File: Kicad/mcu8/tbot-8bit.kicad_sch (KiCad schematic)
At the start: 8 parts

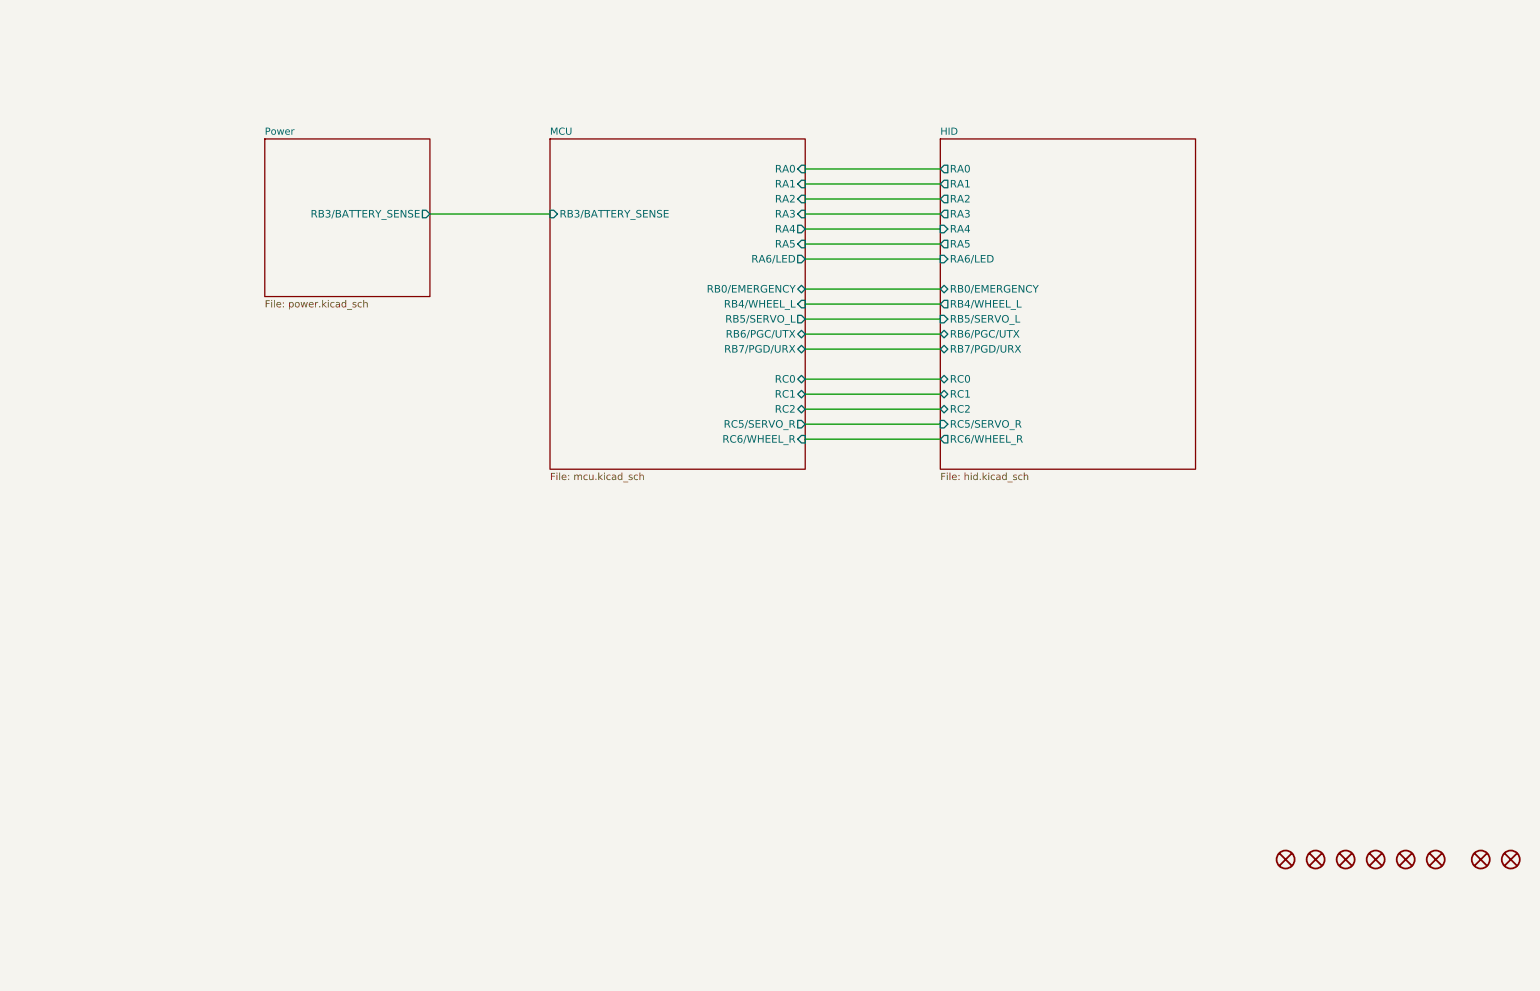
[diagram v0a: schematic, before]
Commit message: Update MCU 8Bit
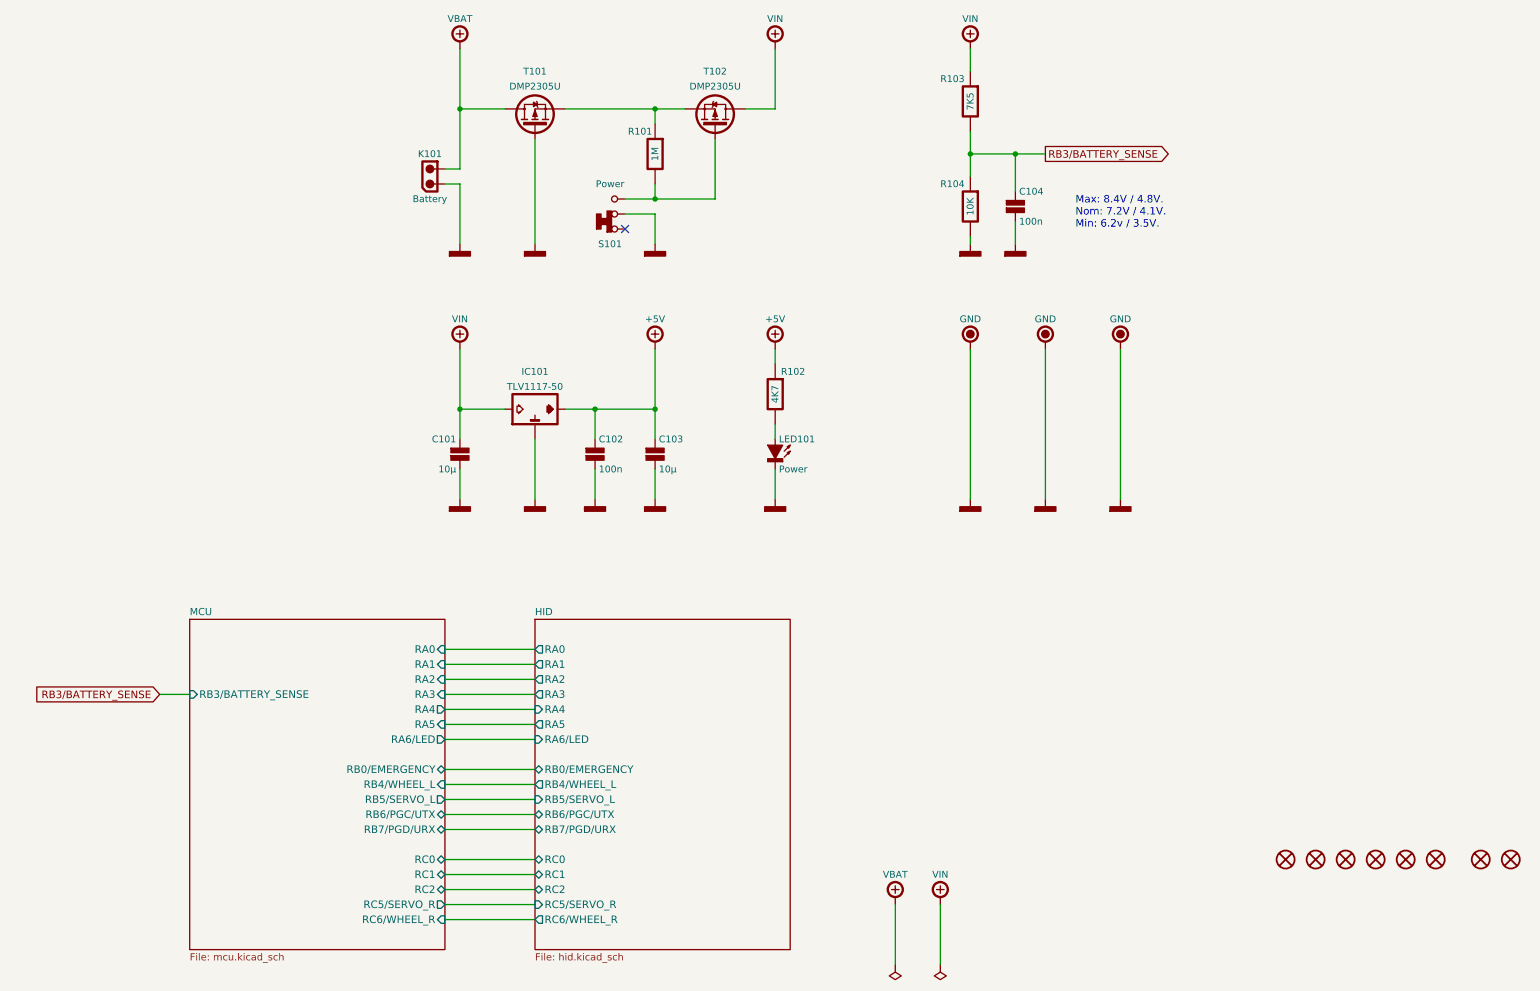
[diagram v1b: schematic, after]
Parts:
- added C101, C103: 10µ, tronixio:CAPACITOR-1206, symbol tronixio:C-1206
- added C102, C104: 100n, tronixio:CAPACITOR-1206, symbol tronixio:C-1206
- added IC101: TLV1117-50, tronixio:SOT-223-3, symbol tronixio:TLV1117-50-SOT
- added K101: Battery, tronixio:MOLEX-22057025, symbol tronixio:MOLEX-MINI-SPOX-02-RIGHT-ANGLE
- added LED101: Power, tronixio:LED-1206, symbol tronixio:LED-1206-PURPLE
- added R101: 1M, tronixio:RESISTOR-1206, symbol tronixio:R-1206
- added R102: 4K7, tronixio:RESISTOR-1206, symbol tronixio:R-1206
- added R103: 7K5, tronixio:RESISTOR-1206, symbol tronixio:R-1206
- added R104: 10K, tronixio:RESISTOR-1206, symbol tronixio:R-1206
- added S101: Power, tronixio:E-SWITCH-200USPXT1A1M2RE, symbol tronixio:E-SWITCH-200USP1T1A1M2RE
- added T101, T102: DMP2305U, tronixio:SOT-23-3, symbol tronixio:DMP2305U-NEW
- added TP101, TP102, TP103: GND, tronixio:KEYSTONE-5006, symbol tronixio:KEYSTONE-5006
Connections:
- new net: LED101.2 (A), R102.1
- new net: R101.1, S101.3, T102.1 (G)
- new net: R101.2, T101.2 (S), T102.2 (S)
- new net +5V: C102.1, C103.1, IC101.2 (VO), R102.2
- new net GND: C101.2, C102.2, C103.2, C104.2, IC101.1 (GND), K101.1, LED101.1 (K), R104.1, S101.2, T101.1 (G), TP101.1, TP102.1, TP103.1
- new net RB3/BATTERY_SENSE: C104.1, R103.1, R104.2
- new net VBAT: K101.2, T101.3 (D)
- new net VIN: C101.1, IC101.3 (VI), R103.2, T102.3 (D)
- no-connect marks 0 -> 1
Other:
- removed sheet Power
- note added: "Max: 8.4V / 4.8V. Nom: 7.2V / 4.1V. Min: 6.2v / 3.5V."

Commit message: Update tbot-8bit.kicad_sch
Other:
- title: Diagram -> Power
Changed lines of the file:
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@@
   (paper "A4")
   (title_block
-    (title "Diagram")
+    (title "Power")
     (date "01/2022")
     (rev "A")
@@
   (sheet_instances
     (path "/" (page "1"))
-    (path "/6012b3a0-2f30-4458-8240-bd443182c6c0" (page "3"))
-    (path "/56bd3a46-de12-45e9-9566-afec966f2cad" (page "4"))
+    (path "/6012b3a0-2f30-4458-8240-bd443182c6c0" (page "2"))
+    (path "/56bd3a46-de12-45e9-9566-afec966f2cad" (page "3"))
   )
   (symbol_instances

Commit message: Update tbot-8bit.kicad_sch
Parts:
- removed TP103: GND, tronixio:KEYSTONE-5006, symbol tronixio:KEYSTONE-5006
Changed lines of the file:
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@@
     (stroke (width 0) (type default) (color 0 0 0 0))
-  )
-  (wire (pts (xy 210.82 86.36) (xy 210.82 111.76))
-    (stroke (width 0) (type solid) (color 0 0 0 0))
   )
   (wire (pts (xy 96.52 139.7) (xy 111.76 139.7))
@@
     )
   )
-  (symbol (lib_id "tronixio:KEYSTONE-5006") (at 210.82 86.36 0) (unit 1)
-    (in_bom yes) (on_board yes)
-    (property "Reference" "TP103" (id 0) (at 210.82 93.98 0)
-      (effects (font (size 1.15 1.15)) hide)
-    )
-    (property "Value" "GND" (id 1) (at 210.82 81.28 0)
-      (effects (font (size 1.15 1.15)))
-    )
-    (property "Footprint" "tronixio:KEYSTONE-5006" (id 2) (at 210.82 96.52 0)
-      (effects (font (size 1 1)) hide)
-    )
-    (property "Datasheet" "https://www.keyelco.com/product.cfm/product_id/1315" (id 3) (at 210.82 99.06 0)
-      (effects (font (size 1 1)) hide)
-    )
-    (property "MOUSER" "534-5006" (id 4) (at 210.82 101.6 0)
-      (effects (font (size 1 1)) hide)
-    )
-    (pin "1")
-  )
   (symbol (lib_id "tronixio:MOUNTING-HOLE-MASK-3MM") (at 264.16 172.72 0) (unit 1)
     (in_bom yes) (on_board yes)
@@
     )
     (property "Datasheet" "" (id 3) (at 99.06 111.76 0)
-      (effects (font (size 1 1)) hide)
-    )
-    (pin "1")
-  )
-  (symbol (lib_id "tronixio:POWER-GND") (at 210.82 111.76 0) (unit 1)
-    (in_bom yes) (on_board yes)
-    (property "Reference" "#PWR0121" (id 0) (at 210.82 118.11 0)
-      (effects (font (size 1 1)) hide)
-    )
-    (property "Value" "GND" (id 1) (at 210.82 115.57 0)
-      (effects (font (size 1 1)) hide)
-    )
-    (property "Footprint" "" (id 2) (at 210.82 111.76 0)
-      (effects (font (size 1 1)) hide)
-    )
-    (property "Datasheet" "" (id 3) (at 210.82 111.76 0)
       (effects (font (size 1 1)) hide)
     )
@@
       (reference "#PWR0120") (unit 1) (value "GND") (footprint "")
     )
-    (path "/63226fa0-632d-4ce6-8a17-8a058e81c611"
-      (reference "#PWR0121") (unit 1) (value "GND") (footprint "")
-    )
     (path "/6012b3a0-2f30-4458-8240-bd443182c6c0/897b9fb4-999f-4b4b-be60-8182d70f5116"
       (reference "#PWR0301") (unit 1) (value "+5V") (footprint "")
@@
       (reference "TP102") (unit 1) (value "GND") (footprint "tronixio:KEYSTONE-5006")
     )
-    (path "/0f01468d-4793-40a9-aa18-d4ec9b5eefff"
-      (reference "TP103") (unit 1) (value "GND") (footprint "tronixio:KEYSTONE-5006")
-    )
-  )
+  )

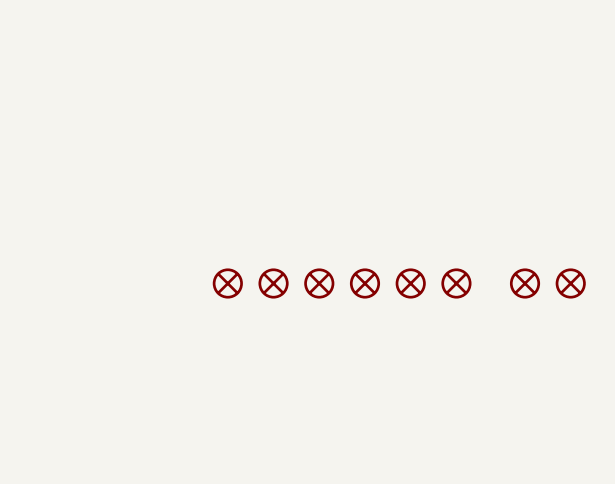
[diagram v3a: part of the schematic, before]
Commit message: Update MCU 8Bit
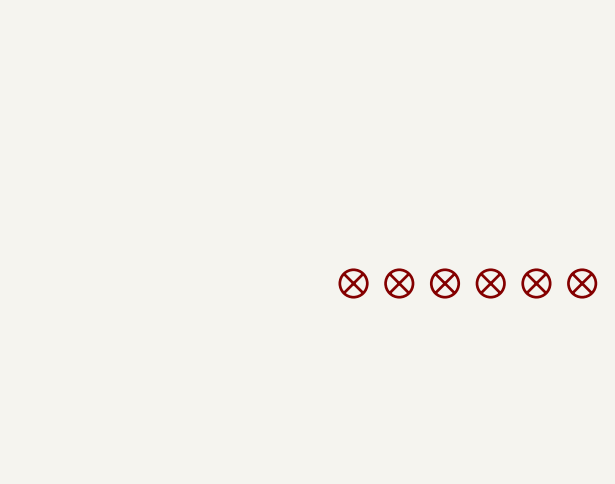
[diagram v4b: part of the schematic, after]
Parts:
- removed H107, H108: MOUNTING-HOLE-3MM, tronixio:M3, symbol tronixio:MOUNTING-HOLE-3MM
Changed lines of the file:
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@@
     )
   )
-  (symbol (lib_id "tronixio:MOUNTING-HOLE-MASK-3MM") (at 264.16 172.72 0) (unit 1)
-    (in_bom yes) (on_board yes)
-    (property "Reference" "H106" (id 0) (at 264.16 167.64 0)
-      (effects (font (size 1 1)) hide)
-    )
-    (property "Value" "MOUNTING-HOLE-MASK-3MM" (id 1) (at 264.16 170.18 0)
-      (effects (font (size 1 1)) hide)
-    )
-    (property "Footprint" "tronixio:M3-MASK" (id 2) (at 264.16 175.26 0)
-      (effects (font (size 1 1)) hide)
-    )
-    (property "Datasheet" "" (id 3) (at 264.16 172.72 0)
+  (symbol (lib_id "tronixio:MOUNTING-HOLE-MASK-3MM") (at 278.13 172.72 0) (unit 1)
+    (in_bom yes) (on_board yes)
+    (property "Reference" "H106" (id 0) (at 278.13 167.64 0)
+      (effects (font (size 1 1)) hide)
+    )
+    (property "Value" "MOUNTING-HOLE-MASK-3MM" (id 1) (at 278.13 170.18 0)
+      (effects (font (size 1 1)) hide)
+    )
+    (property "Footprint" "tronixio:M3-MASK" (id 2) (at 278.13 175.26 0)
+      (effects (font (size 1 1)) hide)
+    )
+    (property "Datasheet" "" (id 3) (at 278.13 172.72 0)
       (effects (font (size 1 1)) hide)
     )
@@
     (pin "1")
   )
-  (symbol (lib_id "tronixio:MOUNTING-HOLE-MASK-3MM") (at 259.08 172.72 0) (unit 1)
-    (in_bom yes) (on_board yes)
-    (property "Reference" "H105" (id 0) (at 259.08 167.64 0)
-      (effects (font (size 1 1)) hide)
-    )
-    (property "Value" "MOUNTING-HOLE-MASK-3MM" (id 1) (at 259.08 170.18 0)
-      (effects (font (size 1 1)) hide)
-    )
-    (property "Footprint" "tronixio:M3-MASK" (id 2) (at 259.08 175.26 0)
-      (effects (font (size 1 1)) hide)
-    )
-    (property "Datasheet" "" (id 3) (at 259.08 172.72 0)
+  (symbol (lib_id "tronixio:MOUNTING-HOLE-MASK-3MM") (at 273.05 172.72 0) (unit 1)
+    (in_bom yes) (on_board yes)
+    (property "Reference" "H105" (id 0) (at 273.05 167.64 0)
+      (effects (font (size 1 1)) hide)
+    )
+    (property "Value" "MOUNTING-HOLE-MASK-3MM" (id 1) (at 273.05 170.18 0)
+      (effects (font (size 1 1)) hide)
+    )
+    (property "Footprint" "tronixio:M3-MASK" (id 2) (at 273.05 175.26 0)
+      (effects (font (size 1 1)) hide)
+    )
+    (property "Datasheet" "" (id 3) (at 273.05 172.72 0)
       (effects (font (size 1 1)) hide)
     )
@@
     (pin "1")
   )
-  (symbol (lib_id "tronixio:MOUNTING-HOLE-MASK-3MM") (at 254 172.72 0) (unit 1)
-    (in_bom yes) (on_board yes)
-    (property "Reference" "H104" (id 0) (at 254 167.64 0)
-      (effects (font (size 1 1)) hide)
-    )
-    (property "Value" "MOUNTING-HOLE-MASK-3MM" (id 1) (at 254 170.18 0)
-      (effects (font (size 1 1)) hide)
-    )
-    (property "Footprint" "tronixio:M3-MASK" (id 2) (at 254 175.26 0)
-      (effects (font (size 1 1)) hide)
-    )
-    (property "Datasheet" "" (id 3) (at 254 172.72 0)
+  (symbol (lib_id "tronixio:MOUNTING-HOLE-MASK-3MM") (at 267.97 172.72 0) (unit 1)
+    (in_bom yes) (on_board yes)
+    (property "Reference" "H104" (id 0) (at 267.97 167.64 0)
+      (effects (font (size 1 1)) hide)
+    )
+    (property "Value" "MOUNTING-HOLE-MASK-3MM" (id 1) (at 267.97 170.18 0)
+      (effects (font (size 1 1)) hide)
+    )
+    (property "Footprint" "tronixio:M3-MASK" (id 2) (at 267.97 175.26 0)
+      (effects (font (size 1 1)) hide)
+    )
+    (property "Datasheet" "" (id 3) (at 267.97 172.72 0)
       (effects (font (size 1 1)) hide)
     )
@@
     (pin "1")
   )
-  (symbol (lib_id "tronixio:MOUNTING-HOLE-3MM") (at 276.86 172.72 0) (unit 1)
-    (in_bom yes) (on_board yes) (fields_autoplaced)
-    (property "Reference" "H108" (id 0) (at 276.86 170.18 0)
-      (effects (font (size 1 1)) hide)
-    )
-    (property "Value" "MOUNTING-HOLE-3MM" (id 1) (at 276.86 175.26 0)
-      (effects (font (size 1 1)) hide)
-    )
-    (property "Footprint" "tronixio:M3" (id 2) (at 276.86 177.8 0)
-      (effects (font (size 1 1)) hide)
-    )
-    (property "Datasheet" "" (id 3) (at 276.86 180.34 0)
-      (effects (font (size 1 1)) hide)
-    )
-  )
   (symbol (lib_id "tronixio:C-1206") (at 193.04 62.23 0) (unit 1)
     (in_bom yes) (on_board yes)
@@
     (pin "1")
   )
-  (symbol (lib_id "tronixio:MOUNTING-HOLE-MASK-3MM") (at 248.92 172.72 0) (unit 1)
-    (in_bom yes) (on_board yes)
-    (property "Reference" "H103" (id 0) (at 248.92 167.64 0)
-      (effects (font (size 1 1)) hide)
-    )
-    (property "Value" "MOUNTING-HOLE-MASK-3MM" (id 1) (at 248.92 170.18 0)
-      (effects (font (size 1 1)) hide)
-    )
-    (property "Footprint" "tronixio:M3-MASK" (id 2) (at 248.92 175.26 0)
-      (effects (font (size 1 1)) hide)
-    )
-    (property "Datasheet" "" (id 3) (at 248.92 172.72 0)
+  (symbol (lib_id "tronixio:MOUNTING-HOLE-MASK-3MM") (at 262.89 172.72 0) (unit 1)
+    (in_bom yes) (on_board yes)
+    (property "Reference" "H103" (id 0) (at 262.89 167.64 0)
+      (effects (font (size 1 1)) hide)
+    )
+    (property "Value" "MOUNTING-HOLE-MASK-3MM" (id 1) (at 262.89 170.18 0)
+      (effects (font (size 1 1)) hide)
+    )
+    (property "Footprint" "tronixio:M3-MASK" (id 2) (at 262.89 175.26 0)
+      (effects (font (size 1 1)) hide)
+    )
+    (property "Datasheet" "" (id 3) (at 262.89 172.72 0)
       (effects (font (size 1 1)) hide)
     )
@@
     (pin "1")
   )
-  (symbol (lib_id "tronixio:MOUNTING-HOLE-3MM") (at 271.78 172.72 0) (unit 1)
-    (in_bom yes) (on_board yes) (fields_autoplaced)
-    (property "Reference" "H107" (id 0) (at 271.78 170.18 0)
-      (effects (font (size 1 1)) hide)
-    )
-    (property "Value" "MOUNTING-HOLE-3MM" (id 1) (at 271.78 175.26 0)
-      (effects (font (size 1 1)) hide)
-    )
-    (property "Footprint" "tronixio:M3" (id 2) (at 271.78 177.8 0)
-      (effects (font (size 1 1)) hide)
-    )
-    (property "Datasheet" "" (id 3) (at 271.78 180.34 0)
-      (effects (font (size 1 1)) hide)
-    )
-  )
   (symbol (lib_id "tronixio:LED-1206-PURPLE") (at 152.4 104.14 270) (mirror x) (unit 1)
     (in_bom yes) (on_board yes)
@@
     (pin "3")
   )
-  (symbol (lib_id "tronixio:MOUNTING-HOLE-MASK-3MM") (at 238.76 172.72 0) (unit 1)
-    (in_bom yes) (on_board yes)
-    (property "Reference" "H101" (id 0) (at 238.76 167.64 0)
-      (effects (font (size 1 1)) hide)
-    )
-    (property "Value" "MOUNTING-HOLE-MASK-3MM" (id 1) (at 238.76 170.18 0)
-      (effects (font (size 1 1)) hide)
-    )
-    (property "Footprint" "tronixio:M3-MASK" (id 2) (at 238.76 175.26 0)
-      (effects (font (size 1 1)) hide)
-    )
-    (property "Datasheet" "" (id 3) (at 238.76 172.72 0)
-      (effects (font (size 1 1)) hide)
-    )
-  )
-  (symbol (lib_id "tronixio:MOUNTING-HOLE-MASK-3MM") (at 243.84 172.72 0) (unit 1)
-    (in_bom yes) (on_board yes)
-    (property "Reference" "H102" (id 0) (at 243.84 167.64 0)
-      (effects (font (size 1 1)) hide)
-    )
-    (property "Value" "MOUNTING-HOLE-MASK-3MM" (id 1) (at 243.84 170.18 0)
-      (effects (font (size 1 1)) hide)
-    )
-    (property "Footprint" "tronixio:M3-MASK" (id 2) (at 243.84 175.26 0)
-      (effects (font (size 1 1)) hide)
-    )
-    (property "Datasheet" "" (id 3) (at 243.84 172.72 0)
+  (symbol (lib_id "tronixio:MOUNTING-HOLE-MASK-3MM") (at 252.73 172.72 0) (unit 1)
+    (in_bom yes) (on_board yes)
+    (property "Reference" "H101" (id 0) (at 252.73 167.64 0)
+      (effects (font (size 1 1)) hide)
+    )
+    (property "Value" "MOUNTING-HOLE-MASK-3MM" (id 1) (at 252.73 170.18 0)
+      (effects (font (size 1 1)) hide)
+    )
+    (property "Footprint" "tronixio:M3-MASK" (id 2) (at 252.73 175.26 0)
+      (effects (font (size 1 1)) hide)
+    )
+    (property "Datasheet" "" (id 3) (at 252.73 172.72 0)
+      (effects (font (size 1 1)) hide)
+    )
+  )
+  (symbol (lib_id "tronixio:MOUNTING-HOLE-MASK-3MM") (at 257.81 172.72 0) (unit 1)
+    (in_bom yes) (on_board yes)
+    (property "Reference" "H102" (id 0) (at 257.81 167.64 0)
+      (effects (font (size 1 1)) hide)
+    )
+    (property "Value" "MOUNTING-HOLE-MASK-3MM" (id 1) (at 257.81 170.18 0)
+      (effects (font (size 1 1)) hide)
+    )
+    (property "Footprint" "tronixio:M3-MASK" (id 2) (at 257.81 175.26 0)
+      (effects (font (size 1 1)) hide)
+    )
+    (property "Datasheet" "" (id 3) (at 257.81 172.72 0)
       (effects (font (size 1 1)) hide)
     )
@@
       (reference "H106") (unit 1) (value "MOUNTING-HOLE-MASK-3MM") (footprint "tronixio:M3-MASK")
     )
-    (path "/a1ff8905-9b82-47d7-be4a-eb2f2eb4d966"
-      (reference "H107") (unit 1) (value "MOUNTING-HOLE-3MM") (footprint "tronixio:M3")
-    )
-    (path "/63d48fd5-e5f1-41b9-bb53-8fbbf91dc3a7"
-      (reference "H108") (unit 1) (value "MOUNTING-HOLE-3MM") (footprint "tronixio:M3")
-    )
     (path "/20e3eb3a-263f-40a8-87e5-fecba4d78c3a"
